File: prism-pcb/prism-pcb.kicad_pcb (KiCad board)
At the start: 4 copper layers, 40 x 40 mm, 39 parts, among them J301 Conn_01x04_P3.5mm_TBH_Horizon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, J401 Molex_Pico-SPOX_Horizontal, M301 Fan_5VDC_25x25x8mm, U301 TPSM365R6V5RDNR, U401 TMC5130A-TA, X401 16MHz

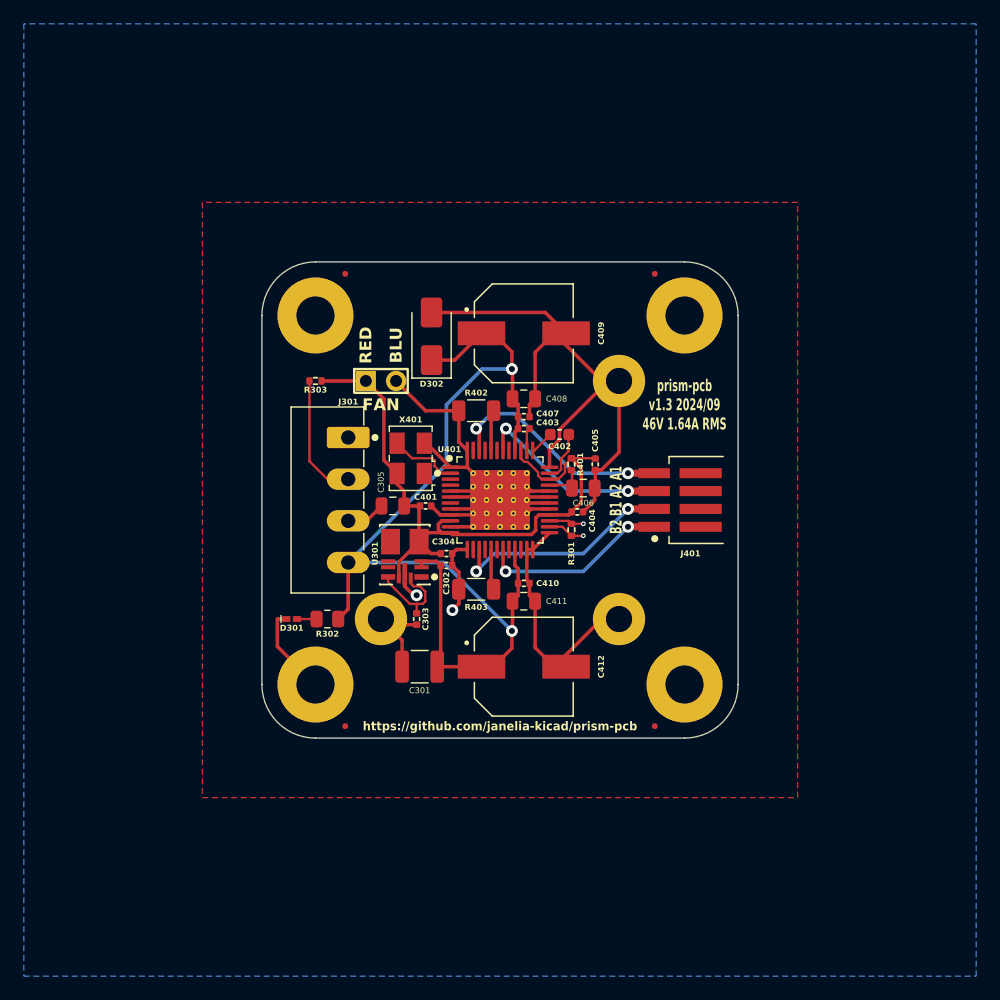
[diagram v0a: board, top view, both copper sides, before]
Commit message: Switch to USB connector
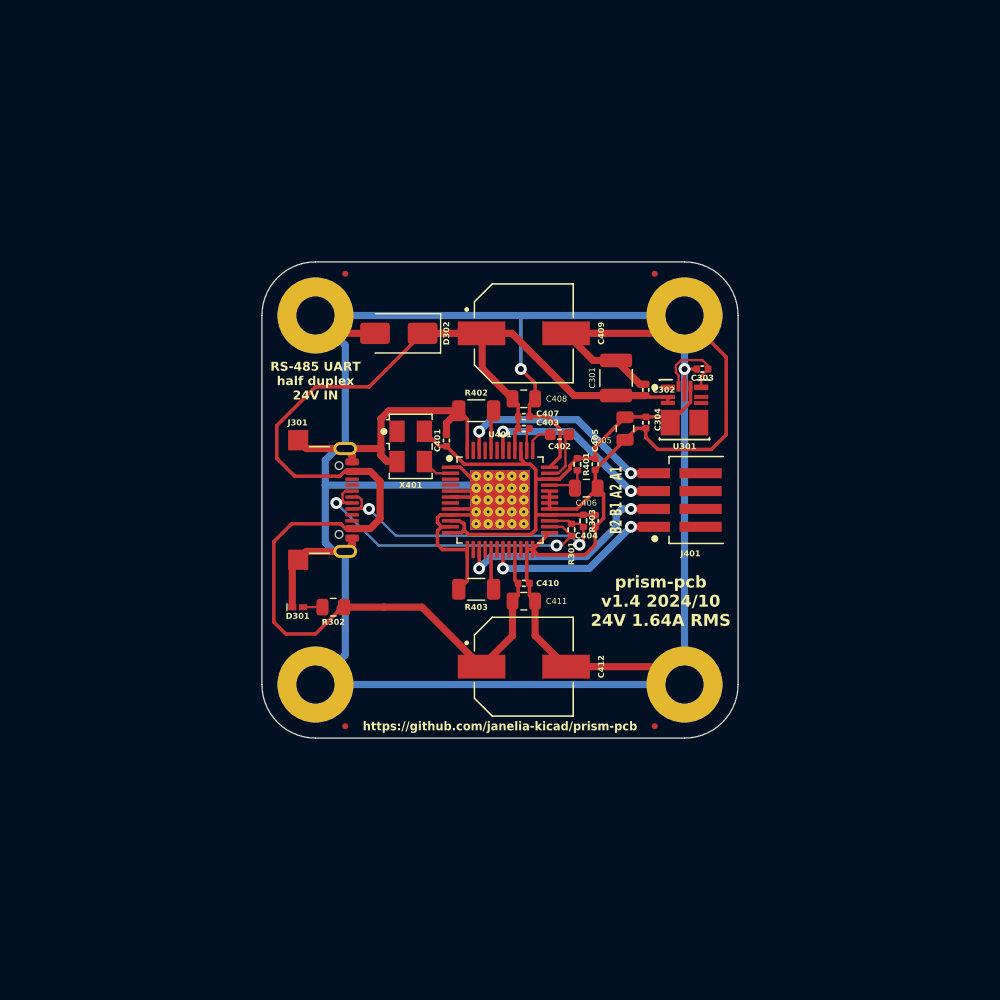
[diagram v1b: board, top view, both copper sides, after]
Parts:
- removed M301: Fan_5VDC_25x25x8mm, Janelia:FAN_5VDC_25x25x8mm
- J301: value Conn_01x04_P3.5mm_TBH_Horizontal_Screw -> Connector_USB_C_Receptacle_USB2.0_16P_GT-USB-7047C; footprint Janelia:PhoenixContact_MC_1,5_4-G-3.5_1x04_P3.50mm_Horizontal_Screw -> Janelia:USB_C_Receptacle_GT-USB-7047C_16P_TopMnt_Horizontal
- R301: value 120 -> 100
- moved C303 31.9 mm to (169.4, 90.6), turned to 180 degrees
- moved C301 29.3 mm to (162.2, 91.3), turned to 90 degrees
- moved U301 26.4 mm to (167.9, 94.1), turned to 0 degrees
- moved R303 25.4 mm to (159.4, 103.3), turned to -90 degrees
- moved C302 22.3 mm to (164.7, 92.3), turned to 90 degrees
- moved C305 20.6 mm to (162.9, 95.6), turned to -90 degrees
- moved C304 20.0 mm to (164.7, 95.1), turned to -90 degrees
- moved C401 5.77 mm to (147.9, 96.6), turned to 90 degrees
- moved D302 2.76 mm to (143.9, 87.6), turned to 180 degrees
- moved C404 1.68 mm to (160.4, 103.3), turned to -90 degrees
- moved D301 1.12 mm to (135.4, 110.6)
- moved R302 1.12 mm to (138.4, 110.6)
- moved X401 1.00 mm to (144.9, 97.1), turned to -90 degrees
- moved R401 0.50 mm to (158.9, 98.6)
- moved C406 0.25 mm to (159.7, 100.6)
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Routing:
- net /VAA: track 87.0 -> 114.3 mm, vias 2 -> 0
- net /SWP: track 39.3 -> 27.4 mm, vias 1 -> 2
- net /+5V: track 57.3 -> 49.6 mm
- net /tmc5130/CLOCK: track 5.81 -> 2.59 mm
- net /GND: track 328.0 -> 325.5 mm
- net /SWN: track 26.3 -> 27.4 mm, vias 1 -> 2
- net /interface/VCC: track 7.99 -> 6.98 mm
- net /tmc5130/BMA1: track 19.5 -> 18.6 mm
- removed copper zone on F.Cu, net /GND
- removed copper zone on In1.Cu, net /GND
- removed copper zone on In2.Cu, net /GND
- removed copper zone on B.Cu, net /VAA
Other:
- copper layers 4 -> 2
- board text added: "RS-485 UART half duplex 24V IN"
- board text added: "prism-pcb v1.4 2024/10 24V 1.64A RMS"
- board text removed: "prism-pcb v1.3 2024/09 46V 1.64A RMS"

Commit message: Finish routing
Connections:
- J301 pad S1: /GND -> unconnected-(J301-SHIELD-PadS1)
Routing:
- net /GND: track 325.5 -> 319.8 mm, vias 2 -> 4
- added copper zone on B.Cu, net /GND
- added copper zone on F.Cu, net /VAA

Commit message: Finish v1.4
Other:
- board text removed: "GND"
- board text removed: "SWN"
- board text removed: "SWP"
- board text removed: "VAA"
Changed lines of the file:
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@@
   (gr_line (start 136.9 81.6) (end 167.9 81.6)
     (stroke (width 0.1) (type default)) (layer "Edge.Cuts"))
-  (gr_text "GND" (at 137.4 103.35 -90) (layer "B.SilkS")
-    (effects (font (size 0.5 0.5) (thickness 0.125) bold) (justify mirror))
-  )
-  (gr_text "VAA" (at 137.4 106.85 -90) (layer "B.SilkS")
-    (effects (font (size 0.5 0.5) (thickness 0.125) bold) (justify mirror))
-  )
-  (gr_text "SWP" (at 137.4 99.85 -90) (layer "B.SilkS")
-    (effects (font (size 0.5 0.5) (thickness 0.125) bold) (justify mirror))
-  )
-  (gr_text "SWN" (at 137.4 96.35 -90) (layer "B.SilkS")
-    (effects (font (size 0.5 0.5) (thickness 0.125) bold) (justify mirror))
-  )
   (gr_text "B2" (at 162.15 103.85 90) (layer "F.SilkS")
     (effects (font (size 1 0.6) (thickness 0.15) bold))
